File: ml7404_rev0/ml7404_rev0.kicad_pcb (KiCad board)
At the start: 4 copper layers, 53.7 x 30.5 mm, 97 parts, among them CN1 MHF-SW23, 20549-001E, CN2 MHF1, 20279-001E-03, U1 SKY13438-374LF, U2 ML7404, U3 BRCB032GWZ-3, U4 BH18PB1WFV

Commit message: pre layout2
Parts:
- removed CN1: MHF-SW23, 20549-001E, ml7404_module:IPEX_20549-001E
- removed PIN21, PIN22, PIN23, PIN24: Conn_01x01, ml7404_module:terminal
- removed R3, R4, R7: 10kΩ, Resistor_SMD:R_0402_1005Metric
- removed RF_Shield1: RF_Sheild_pre, ml7404_module:RF_Shield_pre_29.85x24.0mm
- added CL1: UTC(RF_Shield_Clip), ml7404_module:UTC_RF_Shield_Clip, F.Cu at (117.7, 97.7)
- added CL2: UTC(RF_Shield_Clip), ml7404_module:UTC_RF_Shield_Clip, F.Cu at (132.6, 110.2)
- added RF_shield1: 1500_RF_shield_soldered_recess, ml7404_module:1500_RF_Shield_soldered_30mmx25mm, F.Cu at (132.6, 97.7)
- C1, C10, C11, C12, C13, C14, C15, C16, C17, C18, C19, C2, C20, C21, C22, C23, C24, C25, C26, C27, C28, C29, C3, C30, C31, C32, C33, C34, C35, C36, C37, C38, C4, C41, C5, C6, C7, C8, C9: footprint Capacitor_SMD:C_0402_1005Metric -> ml7404_module:C_0402_1005Metric
- C39, C40: footprint Capacitor_SMD:C_0603_1608Metric -> ml7404_module:C_0603_1608Metric
- L1, L10, L11, L12, L13, L14, L15, L2, L3, L4, L5, L6, L7, L8, L9: footprint Inductor_SMD:L_0402_1005Metric -> ml7404_module:L_0402_1005Metric
- R1, R6, R9: footprint Resistor_SMD:R_0402_1005Metric -> ml7404_module:R_0402_1005Metric
- R5: value N.M. -> 10kΩ; footprint Resistor_SMD:R_0402_1005Metric -> ml7404_module:R_0402_1005Metric
- U3: value BRCB032GWZ-3 -> BR24GxxNUXxx; footprint ml7404_module:BRCB032GWZ-3 -> ml7404_module:BR24GxxNUXxx
- moved PIN11 20.5 mm to (120.1, 114.3), turned to 270 degrees
- moved PIN12 18.5 mm to (122.7, 114.3), turned to 270 degrees
- moved PIN16 17.2 mm to (132.8, 114.3), turned to 270 degrees
- moved PIN13 17.1 mm to (125.2, 114.3), turned to 270 degrees
- moved PIN15 16.4 mm to (130.3, 114.3), turned to 270 degrees
- moved PIN14 16.4 mm to (127.7, 114.3), turned to 270 degrees
- moved PIN17 13.8 mm to (135.4, 114.3)
- moved PIN18 13.8 mm to (137.9, 114.3)
- moved PIN19 13.8 mm to (140.4, 114.3)
- moved PIN20 13.8 mm to (143.0, 114.3)
- moved PIN10 10.5 mm to (120.1, 81.3), turned to 90 degrees
- moved PIN9 9.28 mm to (122.7, 81.3), turned to 90 degrees
- moved PIN1 4.49 mm to (143.0, 81.3)
- moved PIN2 4.49 mm to (140.4, 81.3)
- moved PIN3 4.49 mm to (137.9, 81.3)
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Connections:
- L2 pad 1: Net-(CN1-PadB) -> Net-(C8-Pad1)
- L4 pad 1: Net-(CN1-PadB) -> Net-(C8-Pad1)
- PIN1 pad 1: Net-(PIN1-Pad1) -> GND
- PIN11 pad 1: Net-(PIN11-Pad1) -> GND
- PIN12 pad 1: Net-(PIN12-Pad1) -> RESETN
- PIN13 pad 1: Net-(PIN13-Pad1) -> REGPDIN
- PIN14 pad 1: Net-(PIN14-Pad1) -> SDO
- PIN15 pad 1: RESETN -> SCLK
- PIN16 pad 1: REGPDIN -> SCEN
- PIN17 pad 1: SDO -> SDI
- PIN18 pad 1: SCLK -> GPIO0
- PIN19 pad 1: SCEN -> GPIO1
- PIN20 pad 1: SDI -> GND
- PIN7 pad 1: SCL -> SDA
- PIN8 pad 1: SDA -> SCL
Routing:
- net GND: track 166.0 -> 128.8 mm, vias 348 -> 259
- net +3V3: track 132.7 -> 101.1 mm, vias 26 -> 20
- net Net-(C8-Pad1): track 8.20 -> 18.1 mm
- net Net-(CN1-PadB): track 7.34 -> 0.00 mm
- net SDA: track 16.2 -> 9.21 mm
- net GPIO1: track 16.0 -> 19.5 mm
- net GPIO0: track 14.2 -> 17.5 mm
- net WP: track 10.3 -> 13.6 mm
- net SCL: track 13.0 -> 10.2 mm
- net A2: track 8.48 -> 11.2 mm
- net Net-(ANT1-Pad1): track 7.54 -> 9.17 mm
- net RESETN: track 32.4 -> 33.8 mm
- net SDI: track 16.7 -> 17.3 mm
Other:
- board size 53.7 x 30.5 mm -> 54.2 x 36.6 mm
- rule pad_to_mask_clearance: 0.05 -> 0

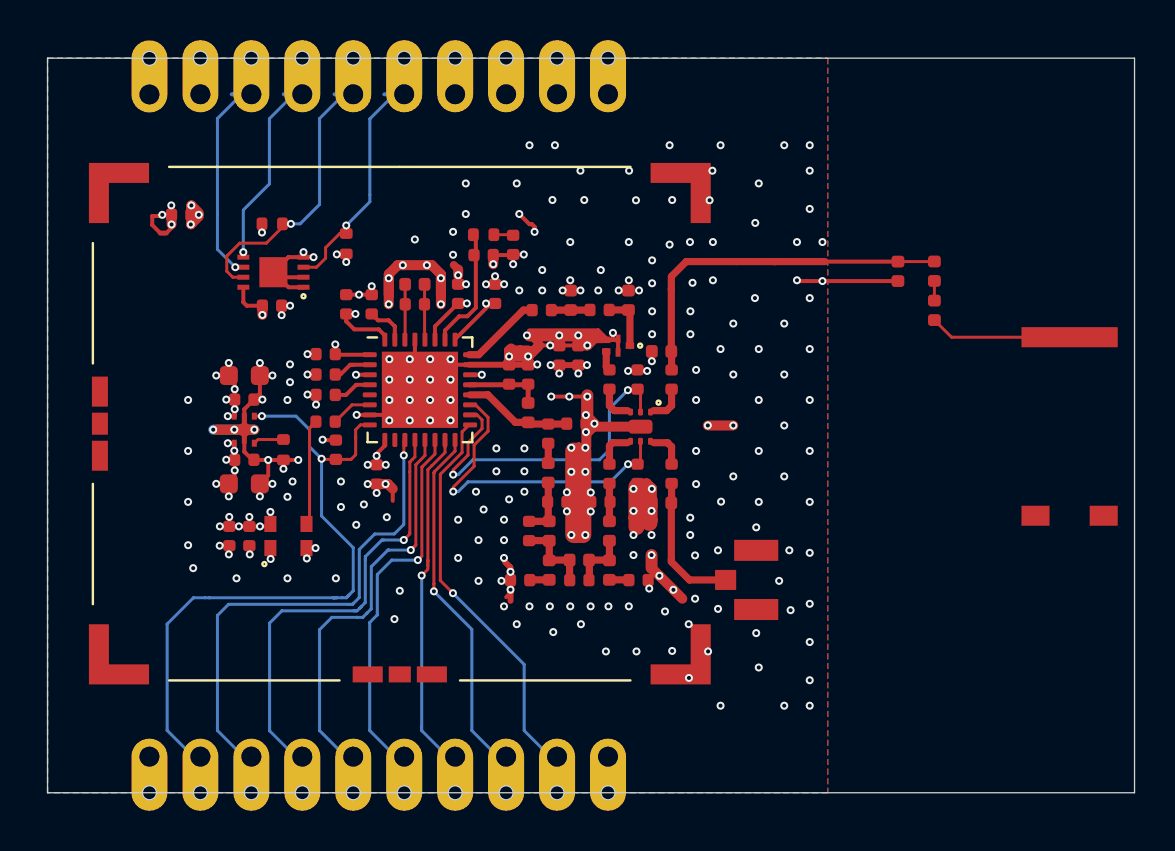
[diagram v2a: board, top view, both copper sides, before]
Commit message: Minor change (Add GND VIA)
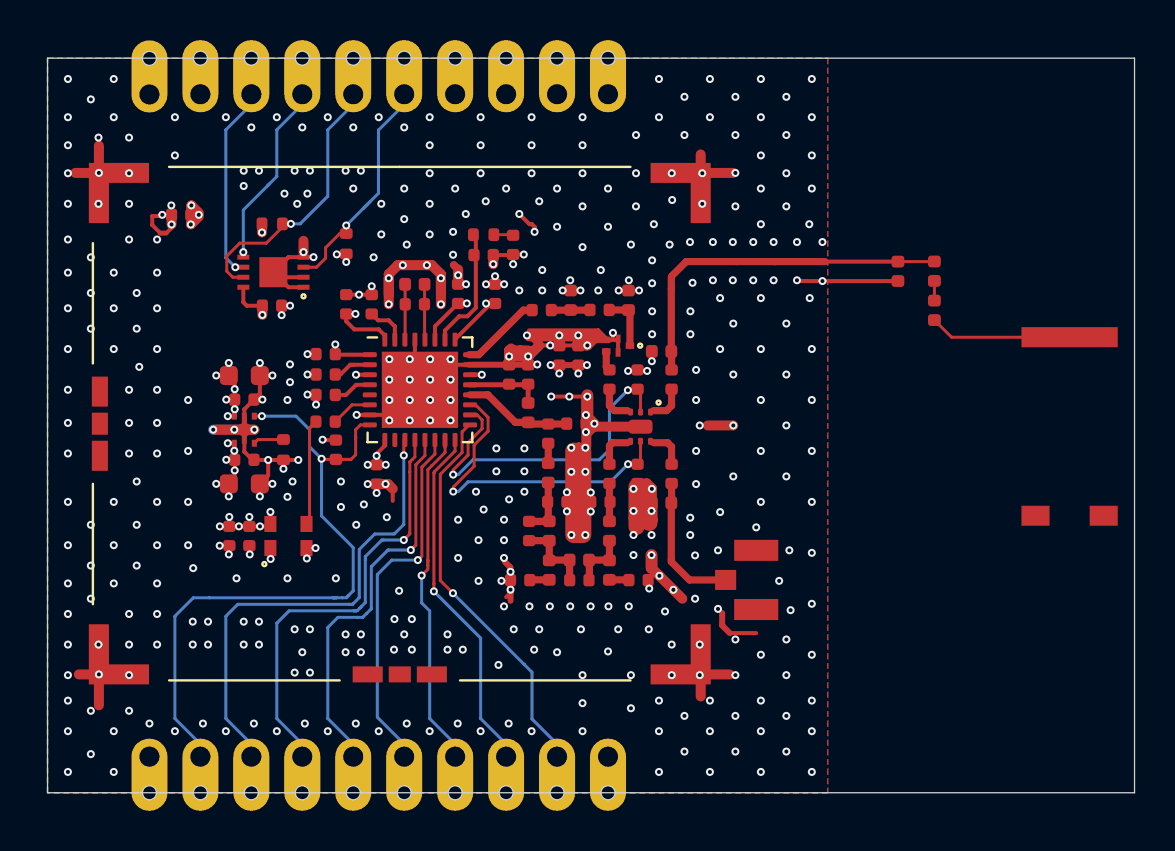
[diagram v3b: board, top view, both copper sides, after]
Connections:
- PIN9 pad : (no net) -> +3V3
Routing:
- net GND: track 128.8 -> 142.3 mm, vias 259 -> 466
- net A2: track 11.2 -> 11.7 mm
- net (no net): vias 0 -> 1

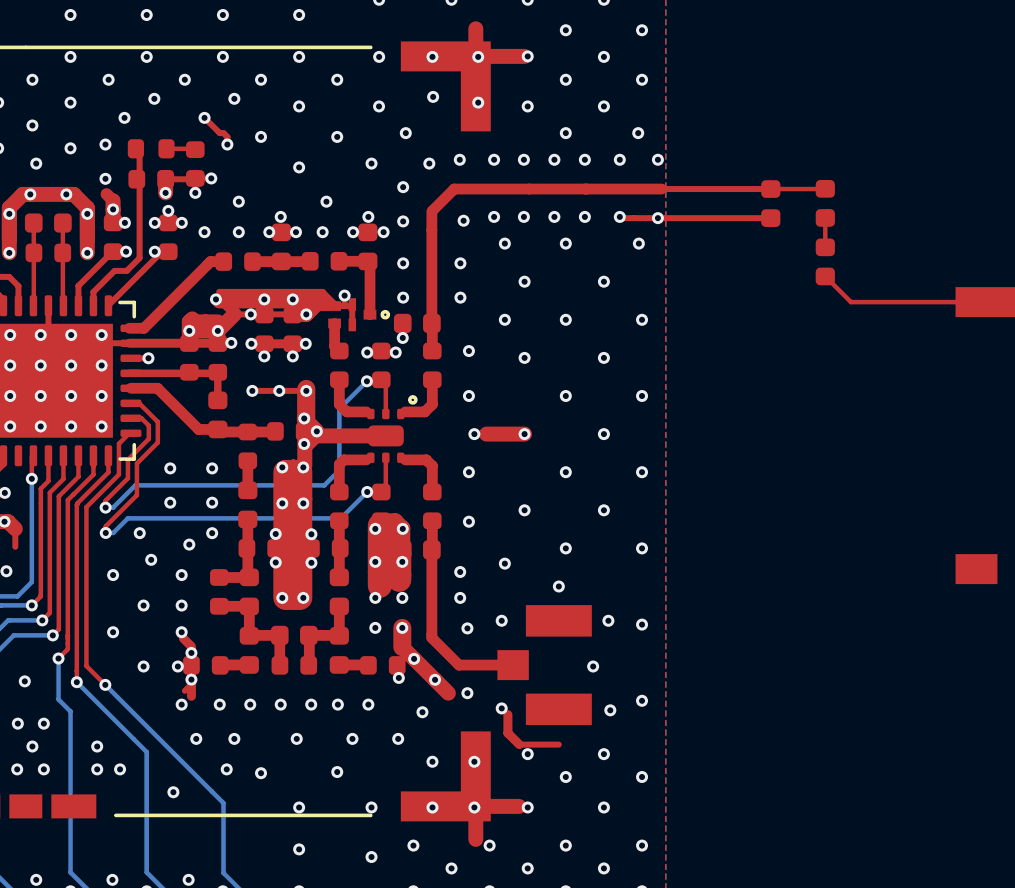
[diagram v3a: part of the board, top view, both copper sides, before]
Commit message: Change RF SMD size 0603
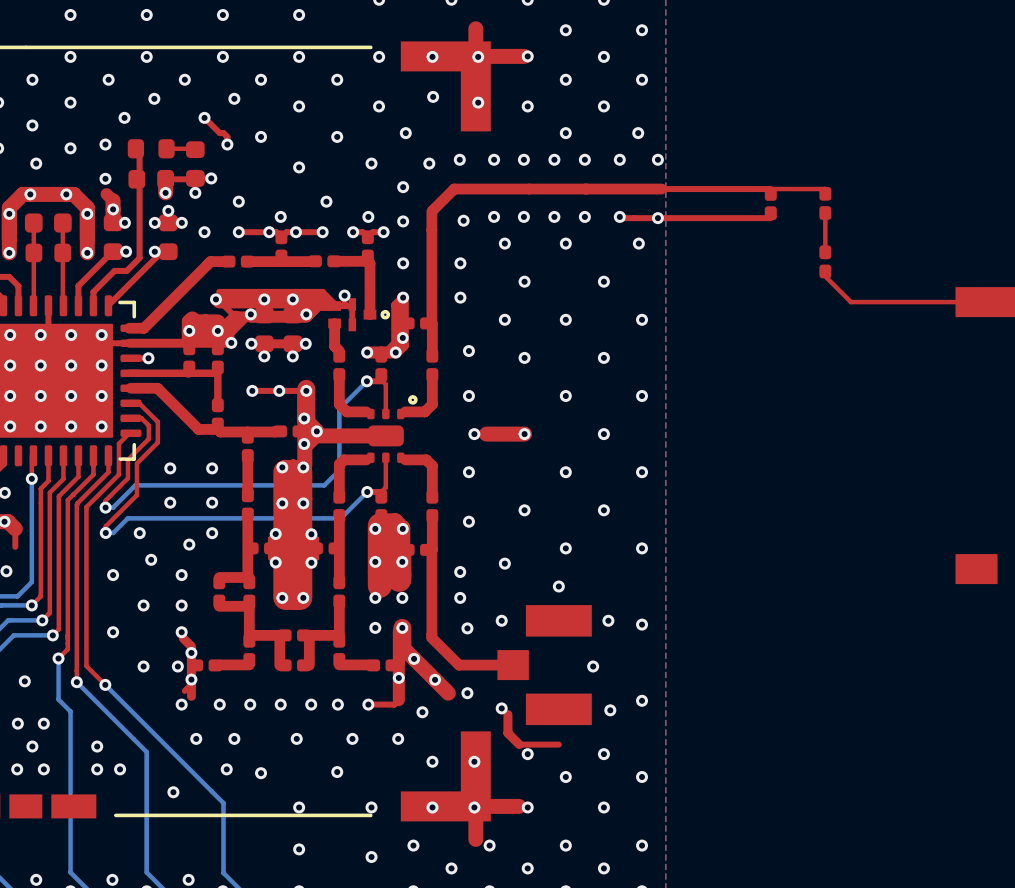
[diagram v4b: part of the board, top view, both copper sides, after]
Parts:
- C14, C15, C16, C17, C19, C20, C21, C23, C24, C26, C27, C29, C30, C31, C32, C33, C41, C8: footprint ml7404_module:C_0402_1005Metric -> ml7404_module:C_0201_0603Metric
- L10, L11, L12, L13, L14, L15, L2, L3, L4, L5, L6, L7, L8, L9: footprint ml7404_module:L_0402_1005Metric -> ml7404_module:L_0201_0603Metric
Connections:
- PIN9 pad : +3V3 -> (no net)
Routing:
- net GND: track 142.3 -> 159.4 mm
